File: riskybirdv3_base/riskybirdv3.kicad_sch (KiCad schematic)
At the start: 176 parts, among them IC1 PMW3901MB-TXQT, J1 USB_B_Micro, J10 Conn_01x05, J11 Conn_01x05, J13 Conn_02x12_Odd_Even_MountingP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, J18 Conn_01x05_MountingPin, J19 Conn_01x30_MountingPin, J2 Conn_01x05, J3 Conn_01x02, J4 Conn_01x02, J5 Conn_01x02, J6 Conn_01x02, J7 Conn_01x02, J8 USB_B_Micro, J9 Conn_01x05, Q1 SI2302, Q2 SI2302, Q3 SI2302, Q4 SI2302, Q8 BC847BDW1, SW1 SW_SPST, SW2 SW_SPST, SW3 SW_SPST, SW4 SW_SPST, U1 ADS7128IRTER, U10 TLV70018DCKR, U12 LP2985-3.0, U13 TPS2113A, U14 ESP32-C6-MINI-1/U, U2 LTC3119EUFD#TRPBF, U3 BMI088, U4 MCP73831-2-OT, U6 FT2232HL-REEL, U7 TPS2113A, U8 FT231XS, U9 VL53L1CXV0FY1, Y1 f

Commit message: riskybirdv3: camera LDOs + front-end parts + off-board debug header
- Camera power: TLV70028 (U7, +2V8/AVDD) + TLV70015 (U11, +1V5/DVDD)
  from +3V3 for HM01B0's 3 domains; decaps at J13.
- Imported to riskybird_lcsc: TPS2117 (4A mux), AON7407 (hi-side P-FET),
  FTSH-110 debug-header footprint (+ earlier LDO symbols/footprints/3D).
- Off-board debug header J1 (FTSH-110-01-L-DV-K, 2x10): FPGA JTAG +
  RISC-V JTAG + console UART + TSI UART, TCK returns GND-flanked.

TODO: J1 VTREF pins (FPGA_VTREF/RV_VTREF) still floating - wire to the
JTAG bank rails once the FPGA VDDIOs are in the schematic.
Note: riskybird_lcsc symbols still easyeda pin-order layout (lib mismatch);
schematic has the readable versions - sync lib->schematic when KiCad closed.
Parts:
- removed C26: 4.7u, Capacitor_SMD:C_0201_0603Metric, symbol Device:C
- removed C34: 1u, Capacitor_SMD:C_0201_0603Metric, symbol Device:C
- removed C35: 0.1u, Capacitor_SMD:C_0402_1005Metric, symbol Device:C
- removed C36: 4.7u, Capacitor_SMD:C_0402_1005Metric, symbol Device:C
- removed C59: 1u, Capacitor_SMD:C_0402_1005Metric, symbol Device:C
- removed D13: LED_BLUE, LED_SMD:LED_0805_2012Metric_Pad1.15x1.40mm_HandSolder, symbol Device:LED
- removed D8, D9: SK6812MINI, LED_SMD:LED_SK6812MINI_PLCC4_3.5x3.5mm_P1.75mm, symbol LED:SK6812MINI
- removed J1: USB_B_Micro, Connector_USB:USB_Micro-B_Molex_47346-0001, symbol Connector:USB_B_Micro
- removed Q8: BC847BDW1, Package_TO_SOT_SMD:SOT-363_SC-70-6, symbol Transistor_BJT:BC847BDW1
- removed R11, R39, R53: 10k, Resistor_SMD:R_0402_1005Metric, symbol Device:R
- removed R21, R24: 27, Resistor_SMD:R_0402_1005Metric, symbol Device:R
- removed R34, R38: 10k, Resistor_SMD:R_0201_0603Metric, symbol Device:R
- removed R37: 150, Resistor_SMD:R_0201_0603Metric, symbol Device:R
- removed R50, R54: 150, Resistor_SMD:R_0402_1005Metric, symbol Device:R
- removed SW3: SW_SPST, Button_Switch_SMD:SW_SPDT_CK_JS102011SAQN, symbol Switch:SW_SPST
- removed U12: LP2985-3.0, Package_TO_SOT_SMD:SOT-23-5, symbol Regulator_Linear:LP2985-3.0
- removed U13, U7: TPS2113A, Package_SO:TSSOP-8_4.4x3mm_P0.65mm, symbol riskybird-rescue:TPS2113A-slice
- removed U8: FT231XS, Package_SO:SSOP-20_3.9x8.7mm_P0.635mm, symbol Interface_USB:FT231XS
- added C47, C48, C49: 10u, Capacitor_SMD:C_0402_1005Metric, symbol Device:C
- added C50, C51, C54: 0.1u, Capacitor_SMD:C_0402_1005Metric, symbol Device:C
- added C52, C53, C55: 1u, Capacitor_SMD:C_0402_1005Metric, symbol Device:C
- added C59, C66: 1uF, Capacitor_SMD:C_0201_0603Metric, symbol Device:C_Small
- added J1: Conn_02x10_Odd_Even, riskybird_lcsc:CONN-SMD_FTSH-110-01-L-DV-K-TR, symbol Connector_Generic:Conn_02x10_Odd_Even
- added Q5: AON7407, riskybird_lcsc:DFN-8_L3.0-W3.0-P0.65-BL, symbol riskybird_lcsc:AON7407
- added R45: 100k, Resistor_SMD:R_0201_0603Metric, symbol Device:R
- added R63, R64, R65, R66: 100, Resistor_SMD:R_0201_0603Metric, symbol Device:R
- added SW5: SW_SPST, Button_Switch_SMD:SW_SPDT_CK_JS102011SAQN, symbol Switch:SW_SPST
- added U11: TLV70015DCKT, riskybird_lcsc:SC-70-5_L2.0-W1.3-P0.65-LS2.1-BR, symbol riskybird_lcsc:TLV70015DCKT
- added U7: TLV70028DCKR, riskybird_lcsc:SC-70-5_L2.1-W1.3-P0.65-LS2.1-BL, symbol riskybird_lcsc:TLV70028DCKR
- added U8: TPS2117DRLR_C22399676, riskybird_lcsc:SOT-583-8_L2.1-W1.2-P0.50-LS1.6-BL, symbol riskybird_lcsc:TPS2117DRLR_C22399676
- C37, C43, C56, C58: footprint Capacitor_SMD:C_0402_1005Metric -> Capacitor_SMD:C_0201_0603Metric
- C44: value 10n -> 0.1u
- C45, C57: value 4.7u -> 0.1u
- R35: value 10k -> 340k; footprint Resistor_SMD:R_0402_1005Metric -> Resistor_SMD:R_0201_0603Metric
- R36: value 10k -> 100k; footprint Resistor_SMD:R_0402_1005Metric -> Resistor_SMD:R_0201_0603Metric
- R40, R51, R52, R55, R56, R57: footprint Resistor_SMD:R_0402_1005Metric -> Resistor_SMD:R_0201_0603Metric
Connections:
- net +3V3_DRONE is gone; now on net +1V5: C57.1
- net DTR is gone; now on an unnamed net: R35.1
- net RTS is gone; now on net GND: R36.1
- net UART1_RX_3V3 is gone; now on net USB_DP: U14.18 (GPIO13/USB_D+)
- net UART1_TX_3V3 is gone; now on net USB_DN: U14.17 (GPIO12/USB_D-)
- net +1V8: now also J13.11 (Pin_11), C51.1, C52.1
- net +3V3: now also U11.1 (IN), U11.3 (EN), U7.1 (IN), U7.3 (EN)
- net +5V: now also C44.1, R35.2, C47.1, U8.3 (VIN1), U8.5 (MODE)
- net +BATT: now also C48.1, C50.1, U8.6 (VIN2)
- net GND: now also J13.1 (Pin_1), J13.10 (Pin_10), J13.13 (Pin_13), J13.15 (Pin_15), J13.3 (Pin_3), C47.2, C48.2, C49.2, C50.2, C51.2, C52.2, C53.2, C54.2, C55.2, C59.2, C66.2, J1.12 (Pin_12), J1.2 (Pin_2), J1.20 (Pin_20), J1.4 (Pin_4), SW5.2 (B), U11.2 (GND), U7.2 (GND), U8.1 (GND)
- net MISO: now also R63.2; no longer U14.24 (GPIO18)
- net MOSI: now also R66.1; no longer U14.16 (MTDO/GPIO7)
- net MOTOR1: now also Q1.1 (G), R15.1, R18.2; no longer R13.1, U14.27 (GPIO21)
- net MOTOR2: now also Q2.1 (G), R13.2, R19.1; no longer R17.1, U14.26 (GPIO20)
- net MOTOR3: now also Q3.1 (G), R16.1, R17.2; no longer R14.1, U14.29 (GPIO23)
- net MOTOR4: now also Q4.1 (G), R14.2, R20.1; no longer R18.1, U14.28 (GPIO22)
- net NCS: now also R64.2; no longer U14.25 (GPIO19)
- net SCL: now also J13.7 (Pin_7)
- net SCLK: now also R65.1; no longer U14.15 (MTCK/GPIO6/ADC1_CH6)
- net SDA: now also J13.8 (Pin_8)
- net VCOM: now also Q5.5 (D), Q5.6 (D), Q5.7 (D), Q5.8 (D), Q5.9 (D)
- net +1V5: now reaches J13.12 (Pin_12)
- net +1V5: now also C55.1, C66.1, U11.5 (OUT)
- net MCLK: now reaches J13.14 (Pin_14)
- net PCLK: now reaches J13.16 (Pin_16)
- net D0: now reaches J13.17 (Pin_17)
- net D1: now reaches J13.18 (Pin_18)
- net D2: now reaches J13.19 (Pin_19)
- net +2V8: now reaches J13.2 (Pin_2)
- net +2V8: now also C53.1, C54.1, C59.1, U7.5 (OUT)
- net D3: now reaches J13.20 (Pin_20)
- net D4: now reaches J13.21 (Pin_21)
- net D5: now reaches J13.22 (Pin_22)
- net D6: now reaches J13.23 (Pin_23)
- net D7: now reaches J13.24 (Pin_24)
- net TRIG: now reaches J13.4 (Pin_4)
- net FVLD: now reaches J13.5 (Pin_5)
- net LVLD: now reaches J13.6 (Pin_6)
- net INT: now reaches J13.9 (Pin_9)
- net at R36.2: now also U8.4 (PR1)
- net +3V3_USB: no longer names the net of C45.1
- net +3V3_USB: now also C49.1, Q5.1 (S), Q5.2 (S), Q5.3 (S), R45.2, U8.2 (VOUT), U8.7 (VOUT)
- new net: Q5.4 (G), R45.1, SW5.1 (A)
- new net: R14.1, U14.28 (GPIO22)
- new net: R65.2, U14.15 (MTCK/GPIO6/ADC1_CH6)
- new net: R13.1, U14.26 (GPIO20)
- new net: R66.2, U14.16 (MTDO/GPIO7)
- new net: R63.1, U14.24 (GPIO18)
- new net: R64.1, U14.25 (GPIO19)
- new net: R18.1, U14.27 (GPIO21)
- new net: R17.1, U14.29 (GPIO23)
- new net FPGA_PROG_B: J1.8 (Pin_8)
- new net FPGA_TCK: J1.3 (Pin_3)
- new net FPGA_TDI: J1.7 (Pin_7)
- new net FPGA_TDO: J1.6 (Pin_6)
- new net FPGA_TMS: J1.5 (Pin_5)
- new net FPGA_VTREF: J1.1 (Pin_1)
- new net RV_TCK: J1.11 (Pin_11)
- new net RV_TDI: J1.14 (Pin_14)
- new net RV_TDO: J1.10 (Pin_10)
- new net RV_TMS: J1.13 (Pin_13)
- new net RV_TRST: J1.15 (Pin_15)
- new net RV_UART_RX: J1.17 (Pin_17)
- new net RV_UART_TX: J1.16 (Pin_16)
- new net RV_VTREF: J1.9 (Pin_9)
- new net TSI_UART_RX: J1.19 (Pin_19)
- new net TSI_UART_TX: J1.18 (Pin_18)
- no-connect marks 16 -> 5
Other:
- note added: "NOTE: AGND"
- note added: "TODO: 1V5"
- note added: "TODO: 2V8"
- moved on the sheet: C37, C43, J13, R52, SW1, SW4

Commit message: riskybirdv3: merge dev B2B/connectors + JB net rename + LSHM footprints
- Hand-reconciled riskybirdv3-dev (B2B JB1/2/3 + off-board connectors)
  into this branch via Eeschema copy (git merge not viable on flat sheet).
- Renamed JB JTAG/UART nets to the J1 debug-header names so header<->B2B
  connect: _2 (bitstream)->FPGA_*, _1->RV_*, UART _1->RV_UART, _2->TSI_UART.
- Assigned Samtec LSHM footprints: JB1/JB2 = LSHM-150 (2x50, C5367357),
  JB3 = LSHM-130 (2x30, C3645597).

TODO: JB shield->GND, J1 VTREF wiring, LSHM hermaphroditic pin offset in
SoM pin-map, RX/TX crossover to sort at the programming board.
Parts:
- removed C18, C19, C20, C21, C22, C24, C25, C27, C29, C31, C33: 100nF, Capacitor_SMD:C_0201_0603Metric, symbol Device:C_Small
- removed C23: 10uF, Capacitor_SMD:C_0201_0603Metric, symbol Device:C_Small
- removed C28, C30: 4.7uF, Capacitor_SMD:C_0201_0603Metric, symbol Device:C_Small
- removed C32: 3.3uF, Capacitor_SMD:C_0201_0603Metric, symbol Device:C_Small
- removed D10, D11, D12: LED, LED_SMD:LED_0402_1005Metric, symbol Device:LED
- removed FB1, FB2: 600R@100MHz/0.5A, Inductor_SMD:L_0603_1608Metric, symbol Device:FerriteBead
- removed J18: Conn_01x05_MountingPin, Connector_JST:JST_ZH_B5B-ZR_1x05_P1.50mm_Vertical, symbol Connector_Generic_MountingPin:Conn_01x05_MountingPin
- removed J19: Conn_01x30_MountingPin, Hirose_FH12-30S-0.5SH_1x30-1MP_P0.50mm_Horizontal, symbol Connector_Generic_MountingPin:Conn_01x30_MountingPin
- removed R26: 1k, Resistor_SMD:R_0201_0603Metric, symbol Device:R_Small
- removed R27, R28, R29: 150, Resistor_SMD:R_0201_0603Metric, symbol Device:R
- removed R5: 12k, Resistor_SMD:R_0201_0603Metric, symbol Device:R_Small
- removed U6: FT2232HL-REEL, Package_QFP:LQFP-64_10x10mm_P0.5mm, symbol dk_Interface-Controllers:FT2232HL-REEL
- removed Y1: f, riskybird:OSC_CSTNE12M0G550000R0, symbol CSTNE12M0G550000R0:CSTNE12M0G550000R0
- JB1, JB2: footprint (none) -> Connector_Samtec:Samtec_LSHM-150-xx.x-x-DV-S_2x50-1SH_P0.50mm_Vertical
- JB3: footprint (none) -> Connector_Samtec:Samtec_LSHM-130-xx.x-x-DV-S_2x30-1SH_P0.50mm_Vertical
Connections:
- net +3V3: now also JB1.14 (Pin_14), JB1.16 (Pin_16)
- net +5V: now also JB1.2 (Pin_2), JB1.4 (Pin_4), JB1.6 (Pin_6), JB2.1 (Pin_1), JB2.3 (Pin_3), JB2.5 (Pin_5), JB2.7 (Pin_7)
- net ACCEL_INT: now also JB1.46 (Pin_46)
- net CamRST: now also JB2.71 (Pin_71)
- net D0: now also JB2.41 (Pin_41)
- net D1: now also JB2.43 (Pin_43)
- net D2: now also JB2.45 (Pin_45)
- net D3: now also JB2.47 (Pin_47)
- net D4: now also JB2.51 (Pin_51)
- net D5: now also JB2.53 (Pin_53)
- net D6: now also JB2.55 (Pin_55)
- net D7: now also JB2.57 (Pin_57)
- net FPGA_TCK: now also JB2.100 (Pin_80)
- net FPGA_TDI: now also JB2.96 (Pin_76)
- net FPGA_TDO: now also JB2.98 (Pin_78)
- net FPGA_TMS: now also JB2.94 (Pin_74)
- net GND: now also JB1.1 (Pin_1), JB1.13 (Pin_13), JB1.19 (Pin_19), JB1.25 (Pin_25), JB1.30 (Pin_30), JB1.33 (Pin_33), JB1.43 (Pin_43), JB1.53 (Pin_53), JB1.54 (Pin_54), JB1.63 (Pin_63), JB1.64 (Pin_64), JB1.7 (Pin_7), JB1.73 (Pin_73), JB1.74 (Pin_74), JB1.83 (Pin_63), JB1.89 (Pin_69), JB1.SH (Shield), JB2.19 (Pin_19), JB2.29 (Pin_29), JB2.30 (Pin_30), JB2.39 (Pin_39), JB2.40 (Pin_40), JB2.49 (Pin_49), JB2.50 (Pin_50), JB2.59 (Pin_59), JB2.60 (Pin_60), JB2.69 (Pin_69), JB2.70 (Pin_70), JB2.79 (Pin_79), JB2.80 (Pin_80), JB2.89 (Pin_69), JB2.SH (Shield), JB3.11 (Pin_11), JB3.12 (Pin_12), JB3.17 (Pin_17), JB3.18 (Pin_18), JB3.23 (Pin_23), JB3.24 (Pin_24), JB3.29 (Pin_29), JB3.30 (Pin_30), JB3.35 (Pin_35), JB3.36 (Pin_36), JB3.45 (Pin_45), JB3.46 (Pin_46), JB3.5 (Pin_5), JB3.55 (Pin_55), JB3.6 (Pin_6), JB3.SH (Shield)
- net GYRO_INT: now also JB1.48 (Pin_48)
- net INT: now also JB2.27 (Pin_27)
- net INT_BARO: now also JB1.52 (Pin_52)
- net LED_N: now also JB2.75 (Pin_75)
- net LVLD: now also JB2.35 (Pin_35)
- net MCLK: now also JB2.33 (Pin_33)
- net MISO: now also JB2.63 (Pin_63)
- net MOSI: now also JB2.65 (Pin_65)
- net MOTION: now also JB2.73 (Pin_73)
- net MOTOR1: now also JB1.32 (Pin_32)
- net MOTOR2: now also JB1.35 (Pin_35)
- net MOTOR3: now also JB1.100 (Pin_80)
- net MOTOR4: now also JB1.99 (Pin_79)
- net NCS: now also JB2.67 (Pin_67)
- net PCLK: now also JB2.37 (Pin_37)
- net RV_TCK: now also JB1.45 (Pin_45)
- net RV_TDI: now also JB1.47 (Pin_47)
- net RV_TDO: now also JB1.49 (Pin_49)
- net RV_TMS: now also JB1.51 (Pin_51)
- net RV_UART_RX: now also JB1.42 (Pin_42)
- net RV_UART_TX: now also JB1.44 (Pin_44)
- net SCL: now also JB2.23 (Pin_23)
- net SCLK: now also JB2.61 (Pin_61)
- net SDA: now also JB2.21 (Pin_21)
- net TOF_Int: now also JB1.50 (Pin_50)
- net TRIG: now also JB2.25 (Pin_25)
- net TSI_UART_RX: now also JB1.91 (Pin_71)
- net TSI_UART_TX: now also JB1.86 (Pin_66)
- net VIOTB: now reaches JB2.10 (Pin_10)
- net VIOTB: now also JB1.10 (Pin_10), JB1.12 (Pin_12), JB2.2 (Pin_2), JB2.4 (Pin_4), JB2.6 (Pin_6), JB2.8 (Pin_8)
- net 3v3OUT: now reaches JB2.11 (Pin_11)
- net 3v3OUT: now also JB2.9 (Pin_9)
- net FLVD: now reaches JB2.31 (Pin_31)
- net FTDI_3v3_2: now reaches JB2.92 (Pin_72)
- net Some_Top_Reset: now reaches JB1.34 (Pin_34)
- net VIDB (1.8V ?): now reaches JB1.40 (Pin_40)
- net VBAT: now reaches JB1.80 (Pin_80)
- no-connect marks 5 -> 151
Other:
- note added: "Left B2B - HR Banks, 3v3 Capable"
- note added: "Right and Top B2Bs - HP Banks, 1v8 Only"
- note added: "SOME TOP RESET"
- note removed: "What is this (SPI/I2C_SEL)"

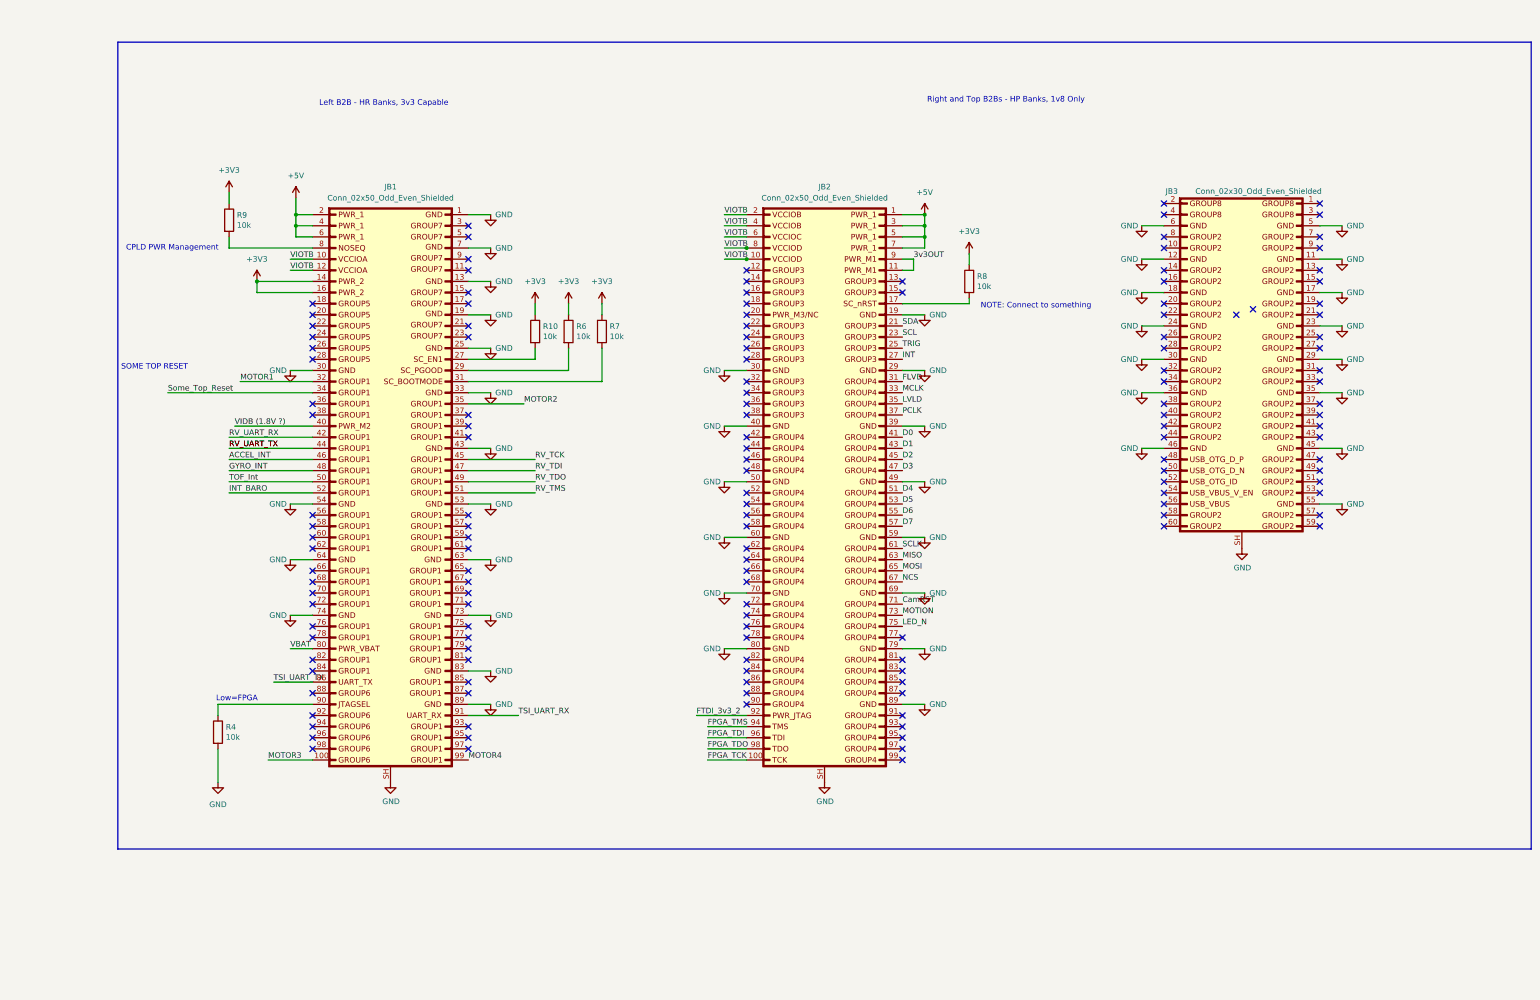
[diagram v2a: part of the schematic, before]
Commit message: add: connector board directory + poka yoke
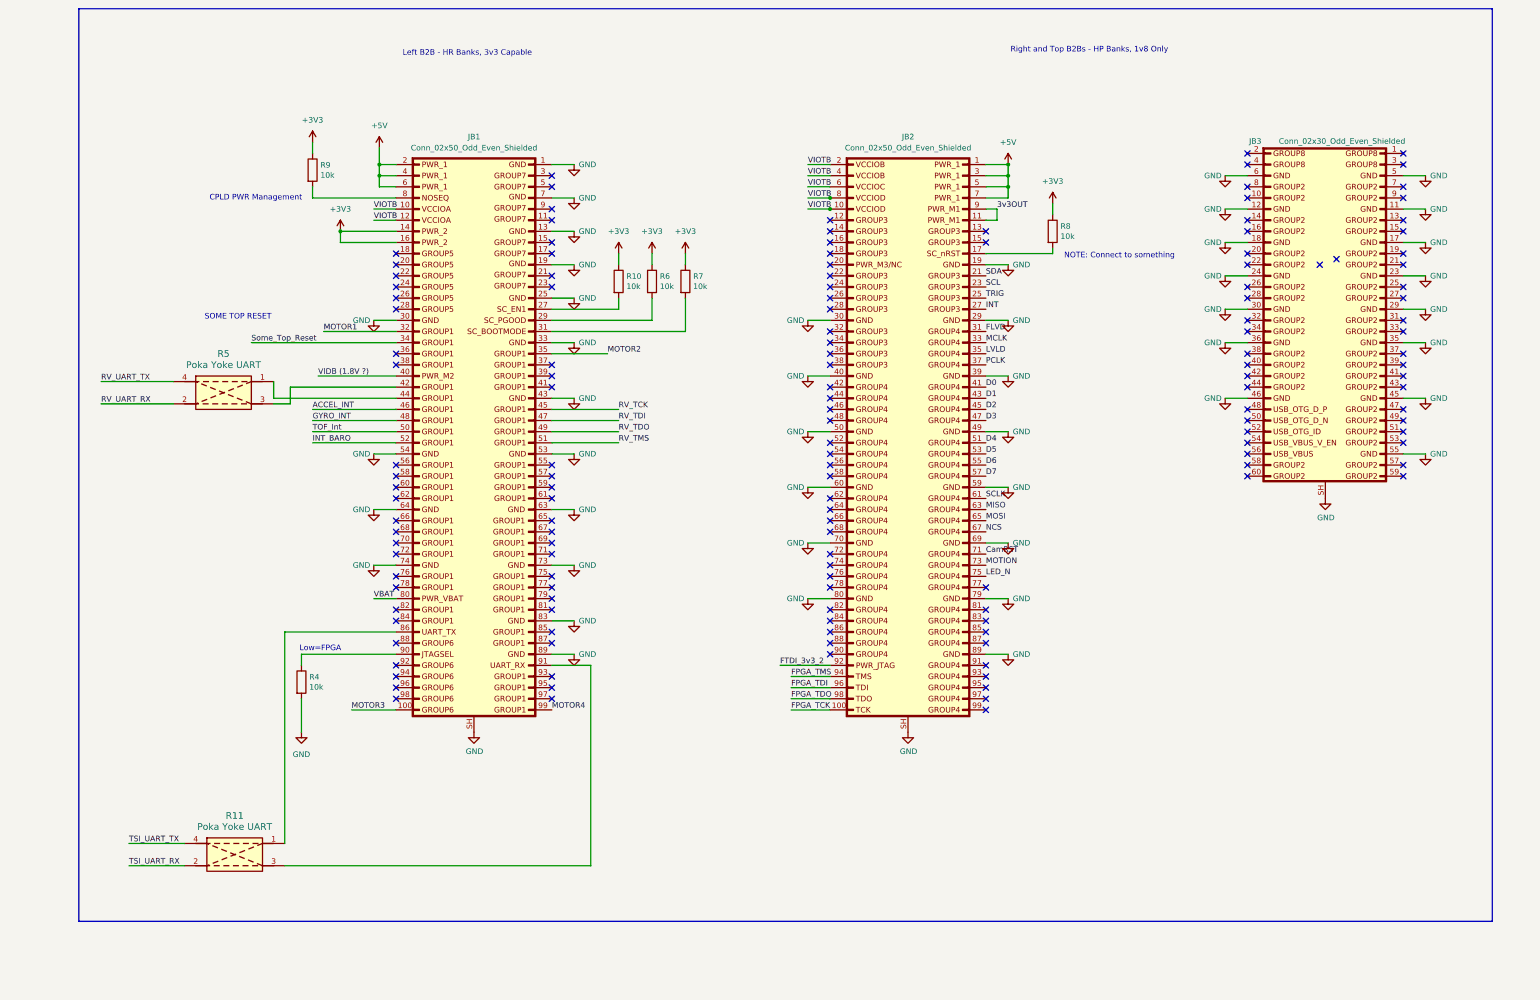
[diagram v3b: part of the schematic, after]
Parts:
- added R11, R5: Poka Yoke UART, symbol poka_yoke_uart:Poka Yoke UART
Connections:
- net RV_UART_RX: now also R5.2; no longer JB1.42 (Pin_42)
- net RV_UART_TX: now also R5.4; no longer JB1.44 (Pin_44)
- net TSI_UART_RX: now also R11.2; no longer JB1.91 (Pin_71)
- net TSI_UART_TX: now also R11.4; no longer JB1.86 (Pin_66)
- new net: JB1.42 (Pin_42), R5.3
- new net: JB1.44 (Pin_44), R5.1
- new net: JB1.86 (Pin_66), R11.1
- new net: JB1.91 (Pin_71), R11.3
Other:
- moved on the sheet: JB1, JB2, JB3, R10, R4, R6, R7, R8, R9
